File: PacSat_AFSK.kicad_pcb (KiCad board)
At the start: 6 copper layers, 92 x 92 mm, 277 parts, among them J2 CONN_02X05, J86 Molex 73251-1153, J87 Molex 73251-1153, P101 U_FL, P651 Conn_04x26_Pin, U13 AS1016204-0108X0PWAY, U156 AX5043, U2 TMS570LS0914PGE, U205 AX5043, U207 TPS22929D, U28 MAX31331TETB+, U305 AX5043, U307 TPS22929D, U405 AX5043, U406 TPS22929D, U505 AX5043, U506 TPS22929D, U604 RBP-140+, U652 CDCLVC1106, U86 TQP7M9106, U87 QPL9547, U88 TCAN1044ADDFRQ1, U89 TPS22917DBV, U90 STWD100NYWY3F, U91 MAX4495ALAUT, U92 MAX4495ALAUT, U93 MAX4495ALAUT, U94 MAX4495ALAUT, U95 STWD100NYWY3F, U96 TPSM828302ARDSR, U97 LP3962EMP-3.3/NOPB, Y26 32.768kHz, Y601 O 16,0-JT22CT-A-P-3,3-LF

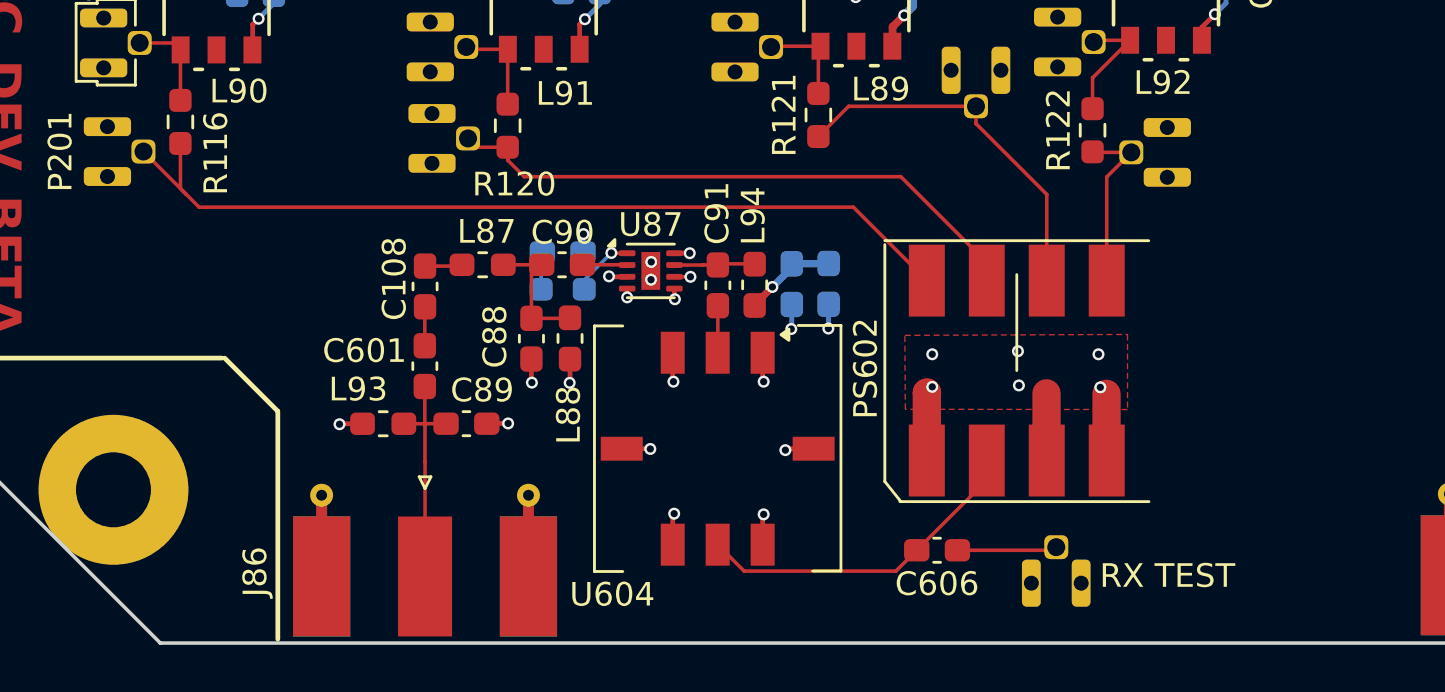
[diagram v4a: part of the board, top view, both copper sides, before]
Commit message: Added a coplaner connection between the RX filter and hybrid
Just playing around to see hard hard it is to draw curved traces and set
up a coplaner.

Signed-off-by: Corey Minyard <corey@minyard.net>
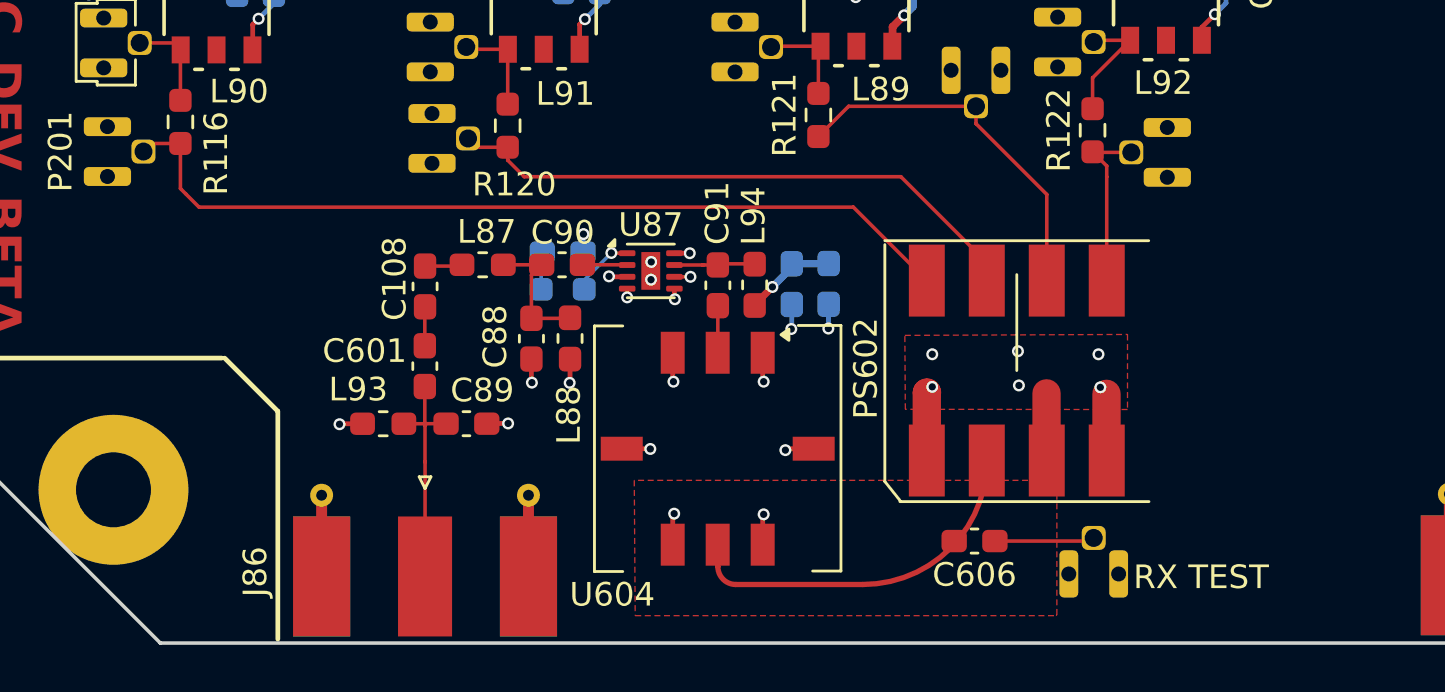
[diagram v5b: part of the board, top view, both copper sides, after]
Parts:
- moved P610 1.63 mm to (198.0, 147.1)
- moved C606 1.63 mm to (193.0, 145.7)
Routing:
- net /Rx_Power_Divider/S+: track 13.5 -> 15.5 mm
- net Port1_P: track 37.7 -> 36.8 mm
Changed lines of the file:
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@@
 	(footprint "Capacitor_SMD:C_0603_1608Metric_Pad1.08x0.95mm_HandSolder"
 		(layer "F.Cu")
-		(at 191.395242 146.070183 180)
+		(at 192.980862 145.68 180)
 		(descr "Capacitor SMD 0603 (1608 Metric), square (rectangular) end terminal, IPC_7351 nominal with elongated pad for handsoldering. (Body size source: IPC-SM-782 page 76, https://www.pcb-3d.com/wordpress/wp-content/uploads/ipc-sm-782a_amendment_1_and_2.pdf), generated with kicad-footprint-generator")
 		(tags "capacitor handsolder")
@@
 	(footprint "PacSatDev_misc:U_FL"
 		(layer "B.Cu")
-		(at 196.4426 147.4636 180)
+		(at 198.02822 147.073417 180)
 		(property "Reference" "P610"
 			(at -3.7774 2.0036 180)
@@
 	)
 	(gr_text "RX TEST"
-		(at 198.278 147.7402 0)
+		(at 199.70462 147.794017 0)
 		(layer "F.SilkS")
 		(effects
@@
 	)
 	(segment
-		(start 183.2226 146.9526)
-		(end 189.650325 146.9526)
-		(width 0.1524)
+		(start 182.11 145.84)
+		(end 182.11 146.76)
+		(width 0.225)
 		(layer "F.Cu")
 		(net 211)
 	)
 	(segment
-		(start 189.650325 146.9526)
-		(end 190.532742 146.070183)
-		(width 0.1524)
+		(start 182.87 147.52)
+		(end 188.25 147.52)
+		(width 0.225)
 		(layer "F.Cu")
 		(net 211)
 	)
-	(segment
-		(start 190.532742 146.070183)
-		(end 193.5 143.102925)
-		(width 0.1524)
+	(arc
+		(start 182.11 146.76)
+		(mid 182.332599 147.297401)
+		(end 182.87 147.52)
+		(width 0.225)
 		(layer "F.Cu")
 		(net 211)
 	)
-	(segment
+	(arc
+		(start 188.25 147.52)
+		(mid 191.962311 145.982311)
+		(end 193.5 142.27)
+		(width 0.225)
+		(layer "F.Cu")
+		(net 211)
+	)
+	(arc
 		(start 182.104 145.834)
-		(end 183.2226 146.9526)
-		(width 0.1524)
+		(mid 182.108243 145.835757)
+		(end 182.11 145.84)
+		(width 0.225)
 		(layer "F.Cu")
 		(net 211)
@@
 	)
 	(segment
-		(start 192.257742 146.070183)
-		(end 196.311017 146.070183)
+		(start 193.843362 145.68)
+		(end 197.896637 145.68)
 		(width 0.1524)
 		(layer "F.Cu")
@@
 	)
 	(segment
+		(start 158.1275 128.8425)
+		(end 157.785 129.185)
+		(width 0.1524)
+		(layer "F.Cu")
+		(net 345)
+	)
+	(segment
 		(start 159.35 128.8425)
-		(end 159.35 130.75)
+		(end 158.1275 128.8425)
 		(width 0.1524)
 		(layer "F.Cu")
@@
 	)
 	(segment
-		(start 159.35 130.75)
-		(end 159.59 130.99)
+		(start 159.35 128.8425)
+		(end 159.35 130.75)
 		(width 0.1524)
 		(layer "F.Cu")
@@
 	)
 	(segment
-		(start 187.85 131.54)
-		(end 160.14 131.54)
+		(start 159.35 130.75)
+		(end 159.59 130.99)
 		(width 0.1524)
 		(layer "F.Cu")
@@
 	)
 	(segment
-		(start 159.59 130.99)
-		(end 157.785 129.185)
+		(start 187.85 131.54)
+		(end 160.14 131.54)
 		(width 0.1524)
 		(layer "F.Cu")
@@
 	)
 	(segment
+		(start 198.58 129.795)
+		(end 197.98 129.195)
+		(width 0.1524)
+		(layer "F.Cu")
+		(net 348)
+	)
+	(segment
 		(start 198.58 130.26)
-		(end 199.62 129.22)
+		(end 198.58 129.795)
 		(width 0.1524)
 		(layer "F.Cu")
@@
 	)
 	(zone
+		(net 1)
+		(net_name "GND")
+		(layer "F.Cu")
+		(hatch edge 0.5)
+		(priority 2)
+		(connect_pads
+			(clearance 0.508)
+		)
+		(min_thickness 0.25)
+		(filled_areas_thickness no)
+		(fill yes
+			(thermal_gap 0.5)
+			(thermal_bridge_width 0.5)
+		)
+		(polygon
+			(pts
+				(xy 178.61 148.84) (xy 196.4378 148.84) (xy 196.468 148.8098) (xy 196.468 143.11) (xy 178.57 143.11)
+			)
+		)
+	)
+	(zone
